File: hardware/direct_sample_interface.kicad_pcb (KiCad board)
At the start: 2 copper layers, 44 parts, among them P1 VHDC_CON, P3 CONN_2X2, P4 CONN_2X2, T1 TRANSFO4, U1 LTC2208, U2 NCP1117

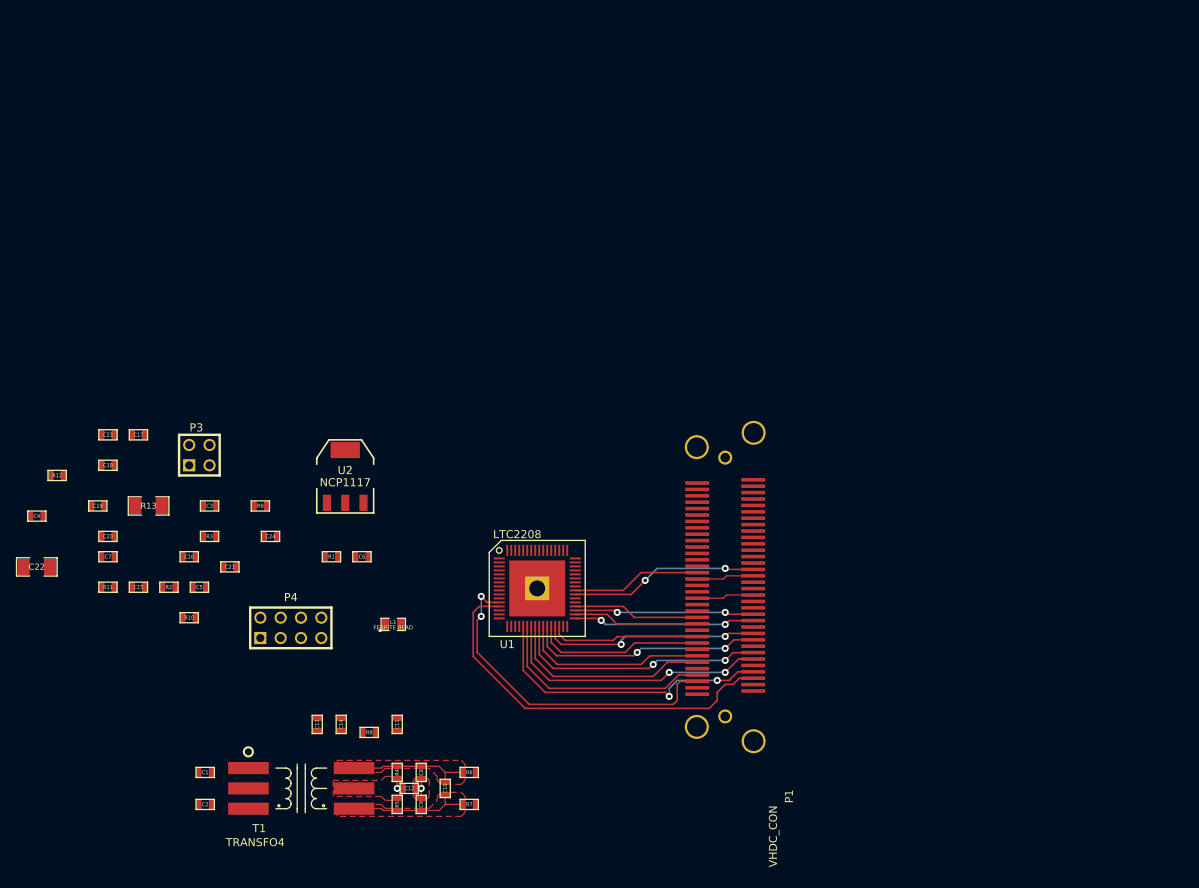
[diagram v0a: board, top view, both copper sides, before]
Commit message: Added/finished hardware designs for direct sample PCB
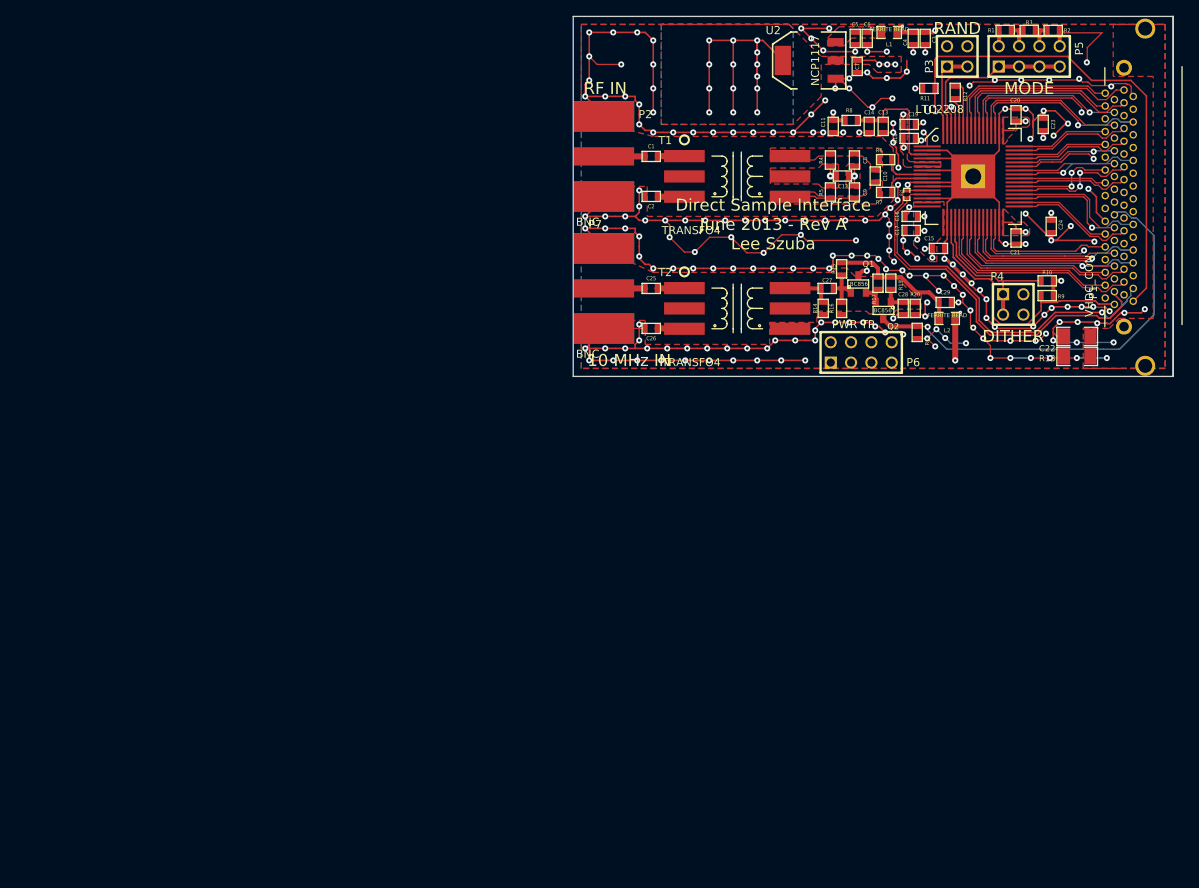
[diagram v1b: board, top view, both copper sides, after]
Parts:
- added C25: C, SM0603, F.Cu at (184.8, 159.5)
- added C26: C, SM0603, F.Cu at (184.8, 164.5)
- added C27: C, SM0603, F.Cu at (206.8, 159.5)
- added C28: C, SM0603, F.Cu at (216.2, 162.0)
- added C29: C, SM0603, F.Cu at (221.5, 161.2)
- added L2: FERRITE BEAD, SM0805, F.Cu at (221.8, 163.2)
- added P2: BNC, EDGE_SMA, F.Cu at (175.0, 143.0)
- added P5: CONN_4X2, pin_array_4x2, F.Cu at (232.0, 130.5)
- added P6: CONN_4X2, pin_array_4x2, F.Cu at (211.0, 167.5)
- added P7: BNC, EDGE_SMA, F.Cu at (175.0, 159.5)
- added Q1: BC856, SOT23, F.Cu at (210.7, 158.9)
- added Q2: BC856, SOT23, F.Cu at (213.8, 162.2)
- added R14: R, SM0603, F.Cu at (206.2, 162.0)
- added R15: R, SM0603, F.Cu at (208.6, 157.1)
- added R16: R, SM0603, F.Cu at (208.6, 162.0)
- added R17: R, SM0603, F.Cu at (213.1, 158.8)
- added R18: R, SM0603, F.Cu at (218.0, 165.0)
- added R19: R, SM0603, F.Cu at (214.7, 158.8)
- added R20: R, SM0603, F.Cu at (217.8, 162.0)
- added R21: R, SM0402, F.Cu at (216.7, 147.8)
- added T2: TRANSFO4, T1-1T, F.Cu at (195.5, 162.0)
- P1: footprint VHDCI_0737760201 -> VHDCI_CON
- P4: footprint pin_array_4x2 -> PIN_ARRAY_2X2
- U2: footprint SOT223 -> SOT223_GND
- moved C22 133.2 mm to (238.0, 165.5), turned to 180 degrees
- moved R2 130.6 mm to (235.0, 127.2), turned to 180 degrees
- moved C20 125.1 mm to (230.3, 137.8), turned to 90 degrees
- moved C4 124.8 mm to (217.5, 128.2), turned to 270 degrees
- moved C23 123.2 mm to (233.8, 139.0), turned to 90 degrees
- moved R12 122.0 mm to (222.8, 135.0), turned to 270 degrees
- moved R3 120.4 mm to (232.0, 127.2), turned to 180 degrees
- moved R11 120.1 mm to (219.4, 134.5), turned to 180 degrees
- moved R13 117.6 mm to (238.0, 168.0), turned to 180 degrees
- moved R10 115.2 mm to (234.2, 158.6)
- moved C19 112.1 mm to (217.0, 139.0)
- moved C7 111.9 mm to (210.5, 131.8), turned to 270 degrees
- moved C15 108.6 mm to (220.7, 154.5)
- moved C18 108.2 mm to (217.0, 140.8)
- moved P3 107.0 mm to (223.0, 130.5)
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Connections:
- P1 pad 20: (no net) -> /REF_CLK
- U1 pad PPAD: (no net) -> AGND
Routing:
- net AGND: track 2.48 -> 620.8 mm, vias 1 -> 216
- net +5V: track 0.00 -> 124.8 mm, vias 0 -> 2
- net /PGA: track 0.00 -> 64.3 mm
- net +3.3VADC: track 0.00 -> 56.8 mm, vias 0 -> 24
- net /REF_CLK: track 0.00 -> 53.6 mm, vias 0 -> 1
- net /SHDN: track 0.00 -> 33.8 mm
- net /~D15: track 0.00 -> 25.0 mm
- net /~D13: track 0.00 -> 24.5 mm, vias 0 -> 1
- net /~D14: track 0.00 -> 24.2 mm
- net /~D12: track 0.00 -> 22.7 mm, vias 0 -> 1
- net /D15: track 0.00 -> 22.4 mm
- net /D14: track 0.00 -> 21.6 mm
- net /MODE: track 0.00 -> 21.4 mm
- net /D13: track 0.00 -> 21.3 mm, vias 0 -> 1
- net /DITH: track 0.00 -> 20.4 mm
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- added copper zone on F.Cu, net +3.3V
- added copper zone on Inner1.Cu, net +3.3V
- added copper zone on B.Cu, net +3.3VADC
- added copper zone on F.Cu, net +3.3VADC
- added copper zone on Inner1.Cu, net +3.3VADC
- added copper zone on F.Cu, net /SHIELD
- added copper zone on F.Cu, net /VREG_IN
- added copper zone on B.Cu, net AGND
- added copper zone on Inner2.Cu, net AGND
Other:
- board outline added: 75 x 45 mm
- copper layers 2 -> 4
- net class Default: clearance 0.2032 -> 0.127; trace_width 0.2032 -> 0.127; via_dia 0.889 -> 0.762; via_drill 0.635 -> 0.3302
- rule trace_clearance: 0.2032 -> 0.127
- rule trace_min: 0.1524 -> 0.127
- rule via_min_drill: 0.508 -> 0.3302
- rule via_min_size: 0.889 -> 0.762
- board text added: "10 MHz IN"
- board text added: "3V3"
- board text added: "5V"
- board text added: "ADC"
- board text added: "CLK DUTY STABILIZER"
- board text added: "DIG"
- board text added: "DIGITAL RANDOMIZER"
- board text added: "DITHER"
- board text added: "Direct Sample Interface June 2013 - Rev A Lee Szuba"
- board text added: "FORMAT"
- board text added: "GND"
- board text added: "MODE"
- board text added: "OFF"
- board text added: "OFF|ON|OFF"
- board text added: "ON"
- board text added: "POWER TEST POINTS"
- board text added: "PWR TP"
- board text added: "RAND"
- board text added: "RF IN"
- board text added: "offset | 2's"
